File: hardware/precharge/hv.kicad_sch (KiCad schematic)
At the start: 41 parts, among them Q1 BC856, Q2 BC856, Q3 BC856, U4 TLV274

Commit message: Preliminary PCB placement
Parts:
- removed C1: 10u, Capacitor_SMD:C_0805_2012Metric, symbol Device:C
- removed C2: 3.3u, Capacitor_SMD:C_0805_2012Metric, symbol Device:C
- added C2: 10u, Capacitor_THT:CP_Radial_D5.0mm_P2.00mm, symbol Device:C_Polarized
- added C4: 3.3u, Capacitor_THT:CP_Radial_D5.0mm_P2.00mm, symbol Device:C_Polarized
- F1: footprint (none) -> footprints:fuseholder
- R25: footprint Resistor_THT:R_Axial_Power_L75.0mm_W9.0mm_P86.36mm -> footprints:HSA50680RJ
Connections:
- net GND: now also C2.2, C4.2
- net at Q1.1 (B), R15.1, R16.1: now also C4.1
- net at R10.1, R11.1, U4.9 (-): now also C2.1
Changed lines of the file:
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@@
     (property "Reference" "R25" (id 0) (at 143.51 30.5775 90))
     (property "Value" "680" (id 1) (at 143.51 33.3526 90))
-    (property "Footprint" "Resistor_THT:R_Axial_Power_L75.0mm_W9.0mm_P86.36mm" (id 2) (at 143.51 33.782 90)
+    (property "Footprint" "footprints:HSA50680RJ" (id 2) (at 143.51 33.782 90)
       (effects (font (size 1.27 1.27)) hide)
     )
@@
     (pin "3")
   )
-  (symbol (lib_id "Device:C") (at 72.39 146.05 0) (unit 1)
-    (in_bom yes) (on_board yes) (fields_autoplaced)
-    (property "Reference" "C1" (id 0) (at 75.311 145.1415 0)
-      (effects (font (size 1.27 1.27)) (justify left))
-    )
-    (property "Value" "10u" (id 1) (at 75.311 147.9166 0)
-      (effects (font (size 1.27 1.27)) (justify left))
-    )
-    (property "Footprint" "Capacitor_SMD:C_0805_2012Metric" (id 2) (at 73.3552 149.86 0)
-      (effects (font (size 1.27 1.27)) hide)
-    )
-    (property "Datasheet" "~" (id 3) (at 72.39 146.05 0)
-      (effects (font (size 1.27 1.27)) hide)
-    )
-    (pin "1")
-    (pin "2")
-  )
   (symbol (lib_id "Device:NetTie_2") (at 49.53 161.29 180) (unit 1)
     (in_bom yes) (on_board yes)
@@
     (property "Reference" "F1" (id 0) (at 121.285 30.8315 90))
     (property "Value" "Fuse" (id 1) (at 121.285 33.6066 90))
-    (property "Footprint" "" (id 2) (at 121.285 37.338 90)
+    (property "Footprint" "footprints:fuseholder" (id 2) (at 121.285 37.338 90)
       (effects (font (size 1.27 1.27)) hide)
     )
@@
     (pin "2")
   )
+  (symbol (lib_id "Device:C_Polarized") (at 90.17 146.05 0) (unit 1)
+    (in_bom yes) (on_board yes) (fields_autoplaced)
+    (property "Reference" "C4" (id 0) (at 93.98 143.8909 0)
+      (effects (font (size 1.27 1.27)) (justify left))
+    )
+    (property "Value" "3.3u" (id 1) (at 93.98 146.4309 0)
+      (effects (font (size 1.27 1.27)) (justify left))
+    )
+    (property "Footprint" "Capacitor_THT:CP_Radial_D5.0mm_P2.00mm" (id 2) (at 91.1352 149.86 0)
+      (effects (font (size 1.27 1.27)) hide)
+    )
+    (property "Datasheet" "~" (id 3) (at 90.17 146.05 0)
+      (effects (font (size 1.27 1.27)) hide)
+    )
+    (pin "1")
+    (pin "2")
+  )
   (symbol (lib_id "Device:R") (at 165.735 43.815 90) (unit 1)
     (in_bom yes) (on_board yes)
@@
     (pin "2")
   )
-  (symbol (lib_id "Device:C") (at 90.17 146.05 0) (unit 1)
-    (in_bom yes) (on_board yes) (fields_autoplaced)
-    (property "Reference" "C2" (id 0) (at 93.091 145.1415 0)
-      (effects (font (size 1.27 1.27)) (justify left))
-    )
-    (property "Value" "3.3u" (id 1) (at 93.091 147.9166 0)
-      (effects (font (size 1.27 1.27)) (justify left))
-    )
-    (property "Footprint" "Capacitor_SMD:C_0805_2012Metric" (id 2) (at 91.1352 149.86 0)
-      (effects (font (size 1.27 1.27)) hide)
-    )
-    (property "Datasheet" "~" (id 3) (at 90.17 146.05 0)
-      (effects (font (size 1.27 1.27)) hide)
-    )
-    (pin "1")
-    (pin "2")
-  )
   (symbol (lib_id "Device:R") (at 133.35 103.505 0) (unit 1)
     (in_bom yes) (on_board yes) (fields_autoplaced)
@@
       (effects (font (size 1.27 1.27)) hide)
     )
+    (pin "1")
+    (pin "2")
+  )
+  (symbol (lib_id "Device:C_Polarized") (at 72.39 146.05 0) (unit 1)
+    (in_bom yes) (on_board yes) (fields_autoplaced)
+    (property "Reference" "C2" (id 0) (at 76.2 143.8909 0)
+      (effects (font (size 1.27 1.27)) (justify left))
+    )
+    (property "Value" "10u" (id 1) (at 76.2 146.4309 0)
+      (effects (font (size 1.27 1.27)) (justify left))
+    )
+    (property "Footprint" "Capacitor_THT:CP_Radial_D5.0mm_P2.00mm" (id 2) (at 73.3552 149.86 0)
+      (effects (font (size 1.27 1.27)) hide)
+    )
+    (property "Datasheet" "~" (id 3) (at 72.39 146.05 0)
+      (effects (font (size 1.27 1.27)) hide)
+    )

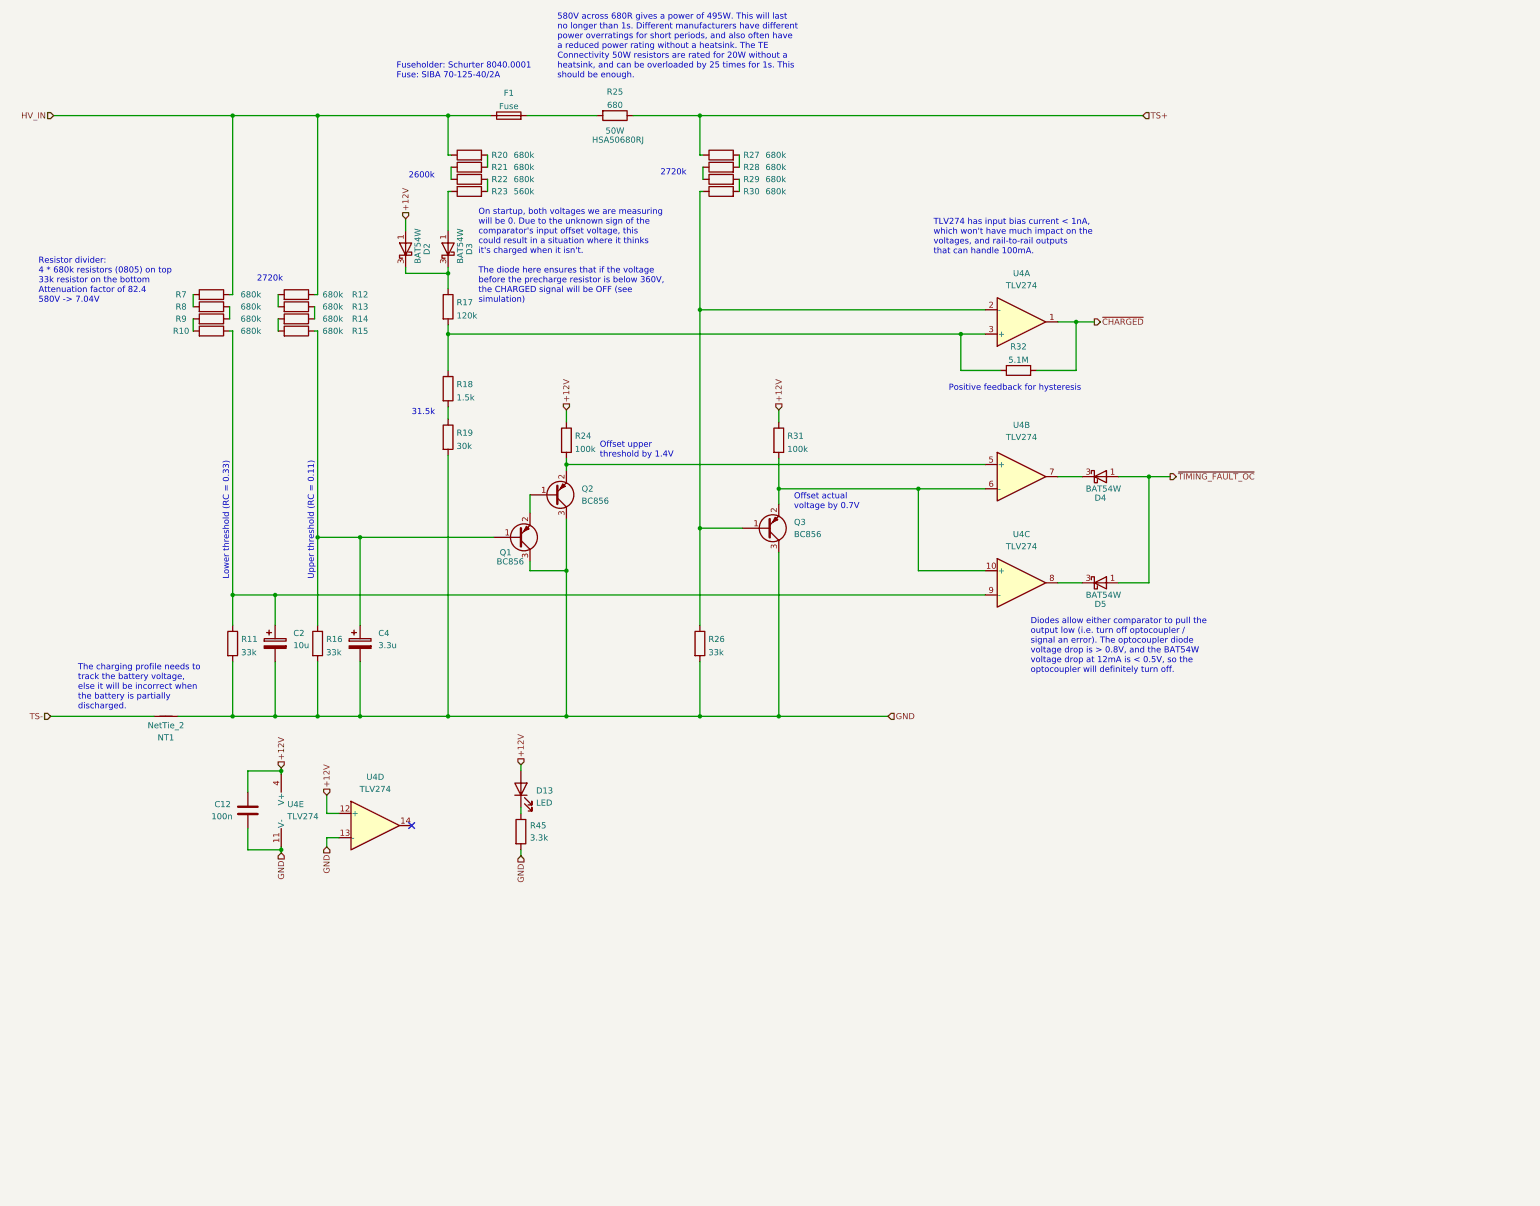
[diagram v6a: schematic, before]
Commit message: Added support for TS_ACTIVE signal, adjusted resistor divider
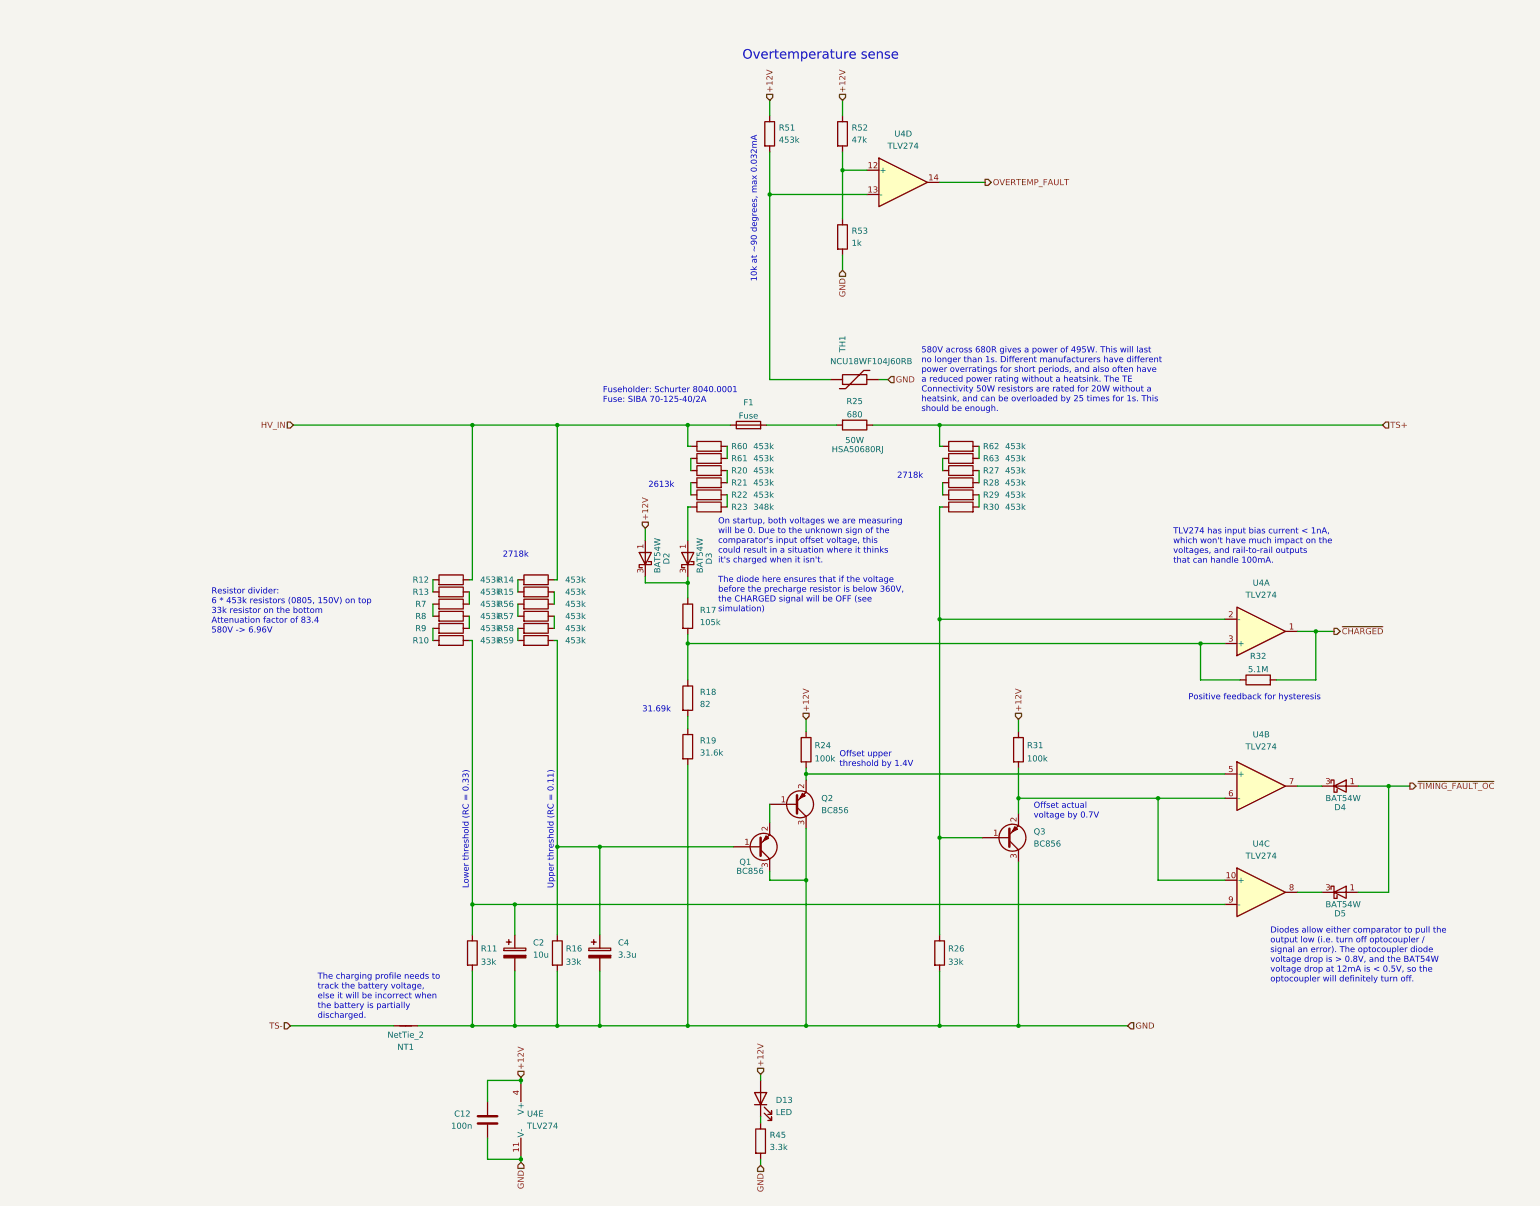
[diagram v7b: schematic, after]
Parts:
- added R51, R56, R57, R58, R59, R60, R61, R62, R63: 453k, Resistor_SMD:R_0805_2012Metric, symbol Device:R
- added R52: 47k, Resistor_SMD:R_0603_1608Metric, symbol Device:R
- added R53: 1k, Resistor_SMD:R_0603_1608Metric, symbol Device:R
- added TH1: NCU18WF104J60RB, Resistor_SMD:R_0603_1608Metric, symbol Device:Thermistor
- R10, R12, R13, R14, R15, R20, R21, R22, R27, R28, R29, R30, R7, R8, R9: value 680k -> 453k
- R17: value 120k -> 105k; footprint Resistor_SMD:R_0603_1608Metric -> Resistor_SMD:R_0805_2012Metric
- R18: value 1.5k -> 82
- R19: value 30k -> 31.6k
- R23: value 560k -> 348k
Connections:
- net +12V: now also R51.1, R52.1; no longer U4.12 (+)
- net GND: now also R53.2, TH1.2; no longer U4.13 (-)
- net HV_IN: now also R14.1, R60.1; no longer R20.1, R7.1
- net TS+: now also R62.1; no longer R27.1
- net at C4.1, Q1.1 (B), R16.1: now also R59.1; no longer R15.1
- net at R13.1: now also R7.1; no longer R14.1
- net OVERTEMP_FAULT: now reaches U4.14
- new net: R27.1, R63.1
- new net: R62.2, R63.2
- new net: R52.2, R53.1, U4.12 (+)
- new net: R51.2, TH1.1, U4.13 (-)
- new net: R15.1, R56.1
- new net: R58.2, R59.2
- new net: R20.1, R61.1
- new net: R60.2, R61.2
- new net: R57.1, R58.1
- new net: R56.2, R57.2
- no-connect marks 1 -> 0
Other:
- note added: "10k at ~90 degrees, max 0.032mA"
- note added: "2613k"
- note added: "2718k"
- note added: "31.69k"
- note added: "Overtemperature sense"
- note added: "Resistor divider: 6 * 453k resistors (0805, 150V) on top 33k resistor on the bottom Attenuation factor of 83.4 580V -> 6.96V"
- note removed: "2600k"
- note removed: "2720k"
- note removed: "31.5k"
- note removed: "Resistor divider: 4 * 680k resistors (0805) on top 33k resistor on the bottom Attenuation factor of 82.4 580V -> 7.04V"
- moved on the sheet: C12, C2, C4, D13, D2, D3, D4, D5, F1, NT1, Q1, Q2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

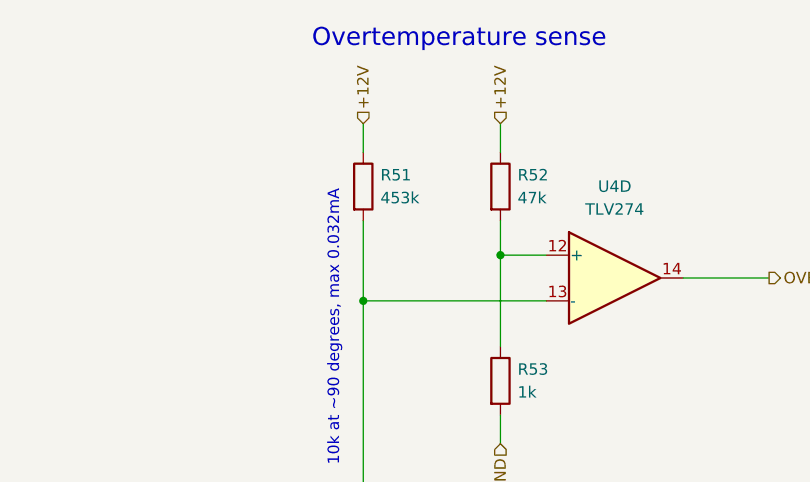
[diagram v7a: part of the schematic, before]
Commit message: Restarted PCB layout
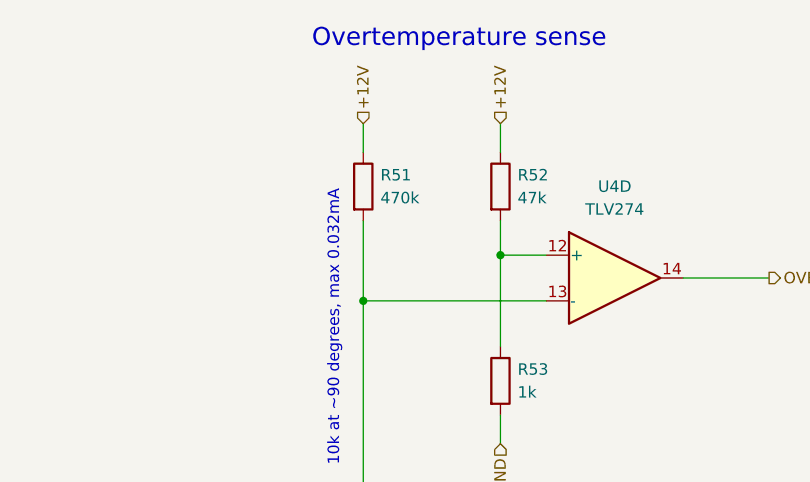
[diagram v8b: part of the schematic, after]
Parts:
- R51: value 453k -> 470k; footprint Resistor_SMD:R_0805_2012Metric -> Resistor_SMD:R_0603_1608Metric
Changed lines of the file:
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@@
       (effects (font (size 1.27 1.27)) (justify left))
     )
-    (property "Value" "453k" (id 1) (at 177.8 40.6399 0)
+    (property "Value" "470k" (id 1) (at 177.8 40.6399 0)
       (effects (font (size 1.27 1.27)) (justify left))
     )
-    (property "Footprint" "Resistor_SMD:R_0805_2012Metric" (id 2) (at 174.117 39.37 90)
+    (property "Footprint" "Resistor_SMD:R_0603_1608Metric" (id 2) (at 174.117 39.37 90)
       (effects (font (size 1.27 1.27)) hide)
     )
